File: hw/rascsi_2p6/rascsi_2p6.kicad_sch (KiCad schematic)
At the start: 88 parts, among them IC1 SN74F245DWR, IC2 SN74F245DWR, IC3 SN74F245DWR, IC4 SN74F245DWR, J1 Raspberry_Pi_2_3, J2 DNP, J4 I2C Pinout, J5 DNP, J6 CONNFLY DB-25, X1 Mac, X2 Dogcow, X3 Mac, X4 Dogcow, X5 Dogcow, X6 Dogcow, X7 Pi, X8 Pi

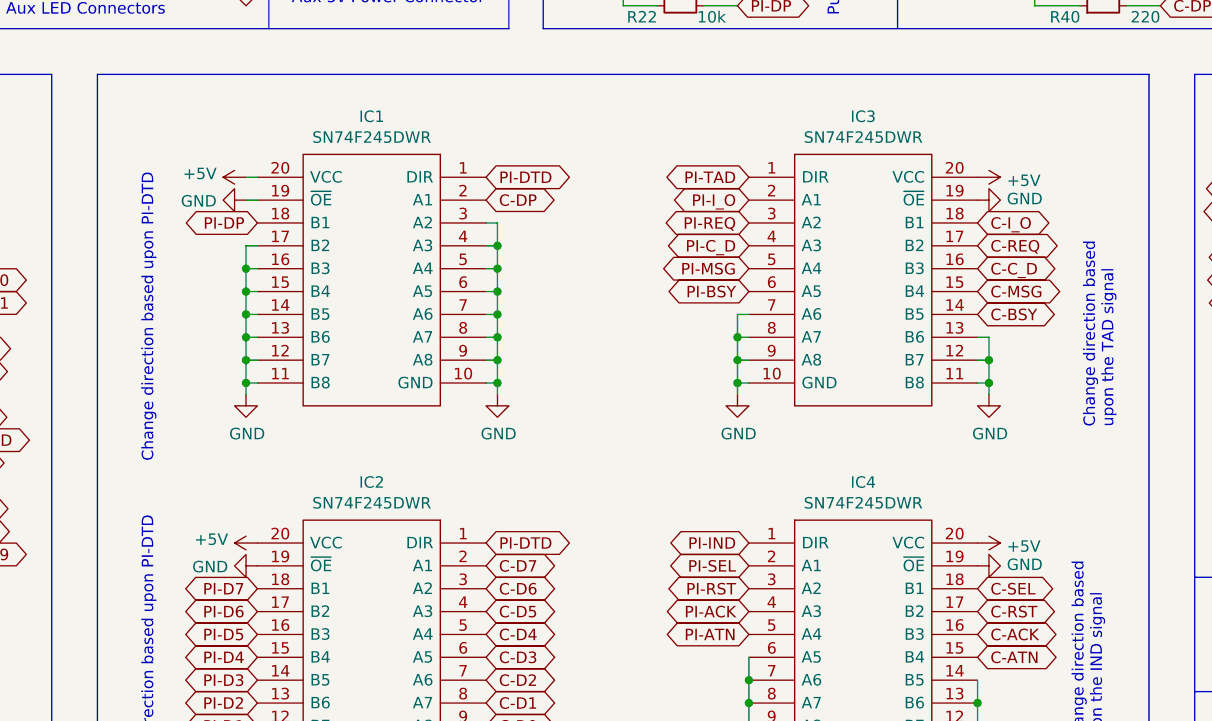
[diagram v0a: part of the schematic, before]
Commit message: Updated to use 3.3v vcc instead of 5v
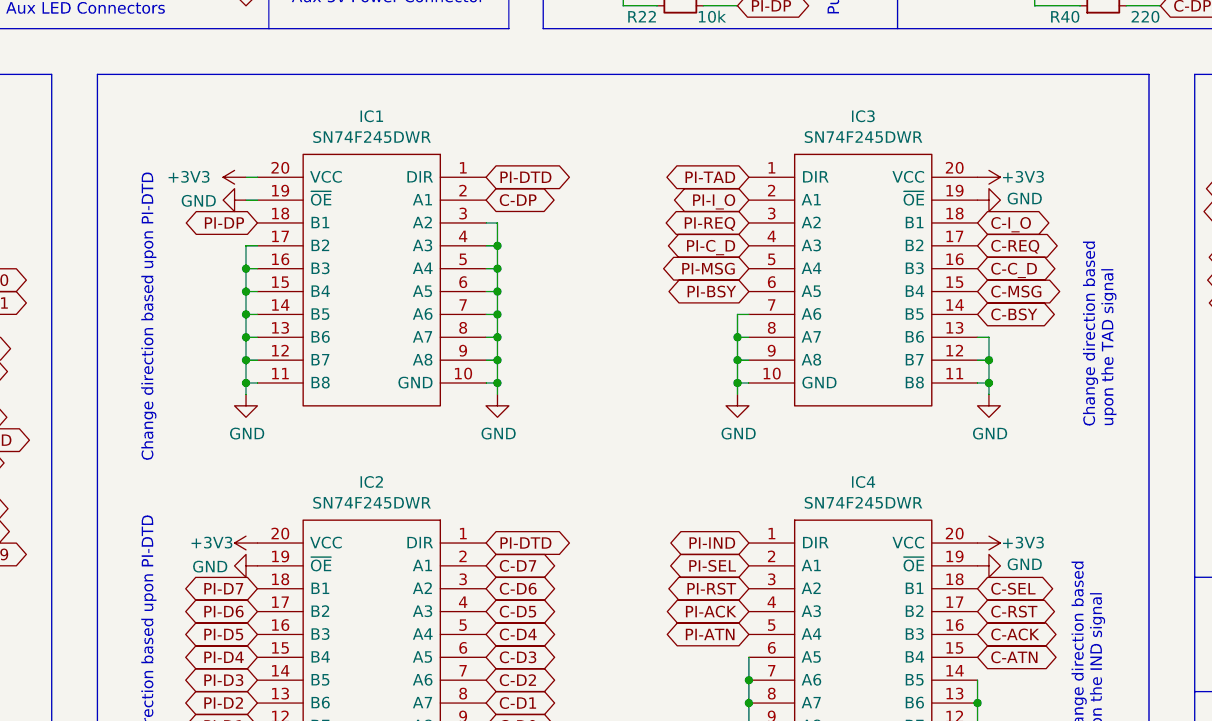
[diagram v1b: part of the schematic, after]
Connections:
- net +3V3: now also IC1.20 (VCC), IC2.20 (VCC), IC3.20 (VCC), IC4.20 (VCC)
- net +5V: no longer IC1.20 (VCC), IC2.20 (VCC), IC3.20 (VCC), IC4.20 (VCC)
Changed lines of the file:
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@@
     (pin "2")
-  )
-  (symbol (lib_id "power:+5V") (at 186.69 78.74 270) (unit 1)
-    (in_bom yes) (on_board yes)
-    (property "Reference" "#PWR028" (id 0) (at 182.88 78.74 0)
-      (effects (font (size 1.27 1.27)) hide)
-    )
-    (property "Value" "+5V" (id 1) (at 189.9412 79.121 90)
-      (effects (font (size 1.27 1.27)) (justify left))
-    )
-    (property "Footprint" "" (id 2) (at 186.69 78.74 0)
-      (effects (font (size 1.27 1.27)) hide)
-    )
-    (property "Datasheet" "" (id 3) (at 186.69 78.74 0)
-      (effects (font (size 1.27 1.27)) hide)
-    )
-    (pin "1")
   )
   (symbol (lib_id "Device:R_Small") (at 153.67 41.91 90) (mirror x) (unit 1)
@@
     (pin "1")
   )
-  (symbol (lib_id "power:+5V") (at 186.69 119.38 270) (unit 1)
-    (in_bom yes) (on_board yes)
-    (property "Reference" "#PWR030" (id 0) (at 182.88 119.38 0)
-      (effects (font (size 1.27 1.27)) hide)
-    )
-    (property "Value" "+5V" (id 1) (at 189.9412 119.761 90)
-      (effects (font (size 1.27 1.27)) (justify left))
-    )
-    (property "Footprint" "" (id 2) (at 186.69 119.38 0)
-      (effects (font (size 1.27 1.27)) hide)
-    )
-    (property "Datasheet" "" (id 3) (at 186.69 119.38 0)
-      (effects (font (size 1.27 1.27)) hide)
-    )
-    (pin "1")
-  )
   (symbol (lib_id "power:GND") (at 187.96 102.87 0) (unit 1)
     (in_bom yes) (on_board yes)
@@
     )
     (property "Datasheet" "" (id 3) (at 36.83 44.45 0)
-      (effects (font (size 1.27 1.27)) hide)
-    )
-    (pin "1")
-  )
-  (symbol (lib_id "power:+5V") (at 105.41 78.74 90) (unit 1)
-    (in_bom yes) (on_board yes)
-    (property "Reference" "#PWR016" (id 0) (at 109.22 78.74 0)
-      (effects (font (size 1.27 1.27)) hide)
-    )
-    (property "Value" "+5V" (id 1) (at 102.1588 78.359 90)
-      (effects (font (size 1.27 1.27)) (justify left))
-    )
-    (property "Footprint" "" (id 2) (at 105.41 78.74 0)
-      (effects (font (size 1.27 1.27)) hide)
-    )
-    (property "Datasheet" "" (id 3) (at 105.41 78.74 0)
-      (effects (font (size 1.27 1.27)) hide)
-    )
-    (pin "1")
-  )
-  (symbol (lib_id "power:+5V") (at 106.68 119.38 90) (unit 1)
-    (in_bom yes) (on_board yes)
-    (property "Reference" "#PWR019" (id 0) (at 110.49 119.38 0)
-      (effects (font (size 1.27 1.27)) hide)
-    )
-    (property "Value" "+5V" (id 1) (at 103.4288 118.999 90)
-      (effects (font (size 1.27 1.27)) (justify left))
-    )
-    (property "Footprint" "" (id 2) (at 106.68 119.38 0)
-      (effects (font (size 1.27 1.27)) hide)
-    )
-    (property "Datasheet" "" (id 3) (at 106.68 119.38 0)
       (effects (font (size 1.27 1.27)) hide)
     )
@@
     (pin "1")
   )
+  (symbol (lib_id "power:+3V3") (at 106.68 119.38 90) (unit 1)
+    (in_bom yes) (on_board yes)
+    (property "Reference" "#PWR0109" (id 0) (at 110.49 119.38 0)
+      (effects (font (size 1.27 1.27)) hide)
+    )
+    (property "Value" "+3V3" (id 1) (at 101.6 119.38 90))
+    (property "Footprint" "" (id 2) (at 106.68 119.38 0)
+      (effects (font (size 1.27 1.27)) hide)
+    )
+    (property "Datasheet" "" (id 3) (at 106.68 119.38 0)
+      (effects (font (size 1.27 1.27)) hide)
+    )
+    (pin "1")
+  )
+  (symbol (lib_id "power:+3V3") (at 186.69 119.38 270) (unit 1)
+    (in_bom yes) (on_board yes)
+    (property "Reference" "#PWR0111" (id 0) (at 182.88 119.38 0)
+      (effects (font (size 1.27 1.27)) hide)
+    )
+    (property "Value" "+3V3" (id 1) (at 191.77 119.38 90))
+    (property "Footprint" "" (id 2) (at 186.69 119.38 0)
+      (effects (font (size 1.27 1.27)) hide)
+    )
+    (property "Datasheet" "" (id 3) (at 186.69 119.38 0)
+      (effects (font (size 1.27 1.27)) hide)
+    )
+    (pin "1")
+  )
   (symbol (lib_id "power:GND") (at 41.91 171.45 180) (unit 1)
     (in_bom yes) (on_board yes)
@@
     )
     (property "Datasheet" "" (id 3) (at 41.91 171.45 0)
+      (effects (font (size 1.27 1.27)) hide)
+    )
+    (pin "1")
+  )
+  (symbol (lib_id "power:+3V3") (at 186.69 78.74 270) (unit 1)
+    (in_bom yes) (on_board yes)
+    (property "Reference" "#PWR0110" (id 0) (at 182.88 78.74 0)
+      (effects (font (size 1.27 1.27)) hide)
+    )
+    (property "Value" "+3V3" (id 1) (at 191.77 78.74 90))
+    (property "Footprint" "" (id 2) (at 186.69 78.74 0)
+      (effects (font (size 1.27 1.27)) hide)
+    )
+    (property "Datasheet" "" (id 3) (at 186.69 78.74 0)
+      (effects (font (size 1.27 1.27)) hide)
+    )
+    (pin "1")
+  )
+  (symbol (lib_id "power:+3V3") (at 105.41 78.74 90) (unit 1)
+    (in_bom yes) (on_board yes)
+    (property "Reference" "#PWR0108" (id 0) (at 109.22 78.74 0)
+      (effects (font (size 1.27 1.27)) hide)
+    )
+    (property "Value" "+3V3" (id 1) (at 99.06 78.74 90))
+    (property "Footprint" "" (id 2) (at 105.41 78.74 0)
+      (effects (font (size 1.27 1.27)) hide)
+    )
+    (property "Datasheet" "" (id 3) (at 105.41 78.74 0)
       (effects (font (size 1.27 1.27)) hide)
     )
@@
       (reference "#PWR015") (unit 1) (value "GND") (footprint "")
     )
-    (path "/00000000-0000-0000-0000-000060b28fd1"
-      (reference "#PWR016") (unit 1) (value "+5V") (footprint "")
-    )
     (path "/00000000-0000-0000-0000-000060b2a4f1"
       (reference "#PWR017") (unit 1) (value "GND") (footprint "")
@@
       (reference "#PWR018") (unit 1) (value "GND") (footprint "")
     )
-    (path "/00000000-0000-0000-0000-000060b29986"
-      (reference "#PWR019") (unit 1) (value "+5V") (footprint "")
-    )
     (path "/00000000-0000-0000-0000-000060b29f0d"
       (reference "#PWR020") (unit 1) (value "GND") (footprint "")
@@
       (reference "#PWR027") (unit 1) (value "GND") (footprint "")
     )
-    (path "/00000000-0000-0000-0000-00005f4fa641"
-      (reference "#PWR028") (unit 1) (value "+5V") (footprint "")
-    )
     (path "/00000000-0000-0000-0000-0000607125c6"
       (reference "#PWR029") (unit 1) (value "GND") (footprint "")
     )
-    (path "/00000000-0000-0000-0000-00006066bbdb"
-      (reference "#PWR030") (unit 1) (value "+5V") (footprint "")
-    )
     (path "/00000000-0000-0000-0000-000060637f3a"
       (reference "#PWR031") (unit 1) (value "GND") (footprint "")
@@
       (reference "#PWR0107") (unit 1) (value "GND") (footprint "")
     )
+    (path "/b377b1ca-88e6-43be-a10a-a568d8ee054d"
+      (reference "#PWR0108") (unit 1) (value "+3V3") (footprint "")
+    )
+    (path "/855aacd5-f781-4022-aad5-a068639eb9c3"
+      (reference "#PWR0109") (unit 1) (value "+3V3") (footprint "")
+    )
+    (path "/af9902e1-e19a-4f95-8ec4-94b31bd1b919"
+      (reference "#PWR0110") (unit 1) (value "+3V3") (footprint "")
+    )
+    (path "/9ec9cb57-10a3-411e-bf1b-a9446aae1b17"
+      (reference "#PWR0111") (unit 1) (value "+3V3") (footprint "")
+    )
     (path "/00000000-0000-0000-0000-00005ef6e9e0"
